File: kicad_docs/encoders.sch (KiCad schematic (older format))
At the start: 40 parts, among them SW1 Rotary_Encoder_Switch, SW2 Rotary_Encoder_Switch, SW3 Rotary_Encoder_Switch, SW4 Rotary_Encoder_Switch

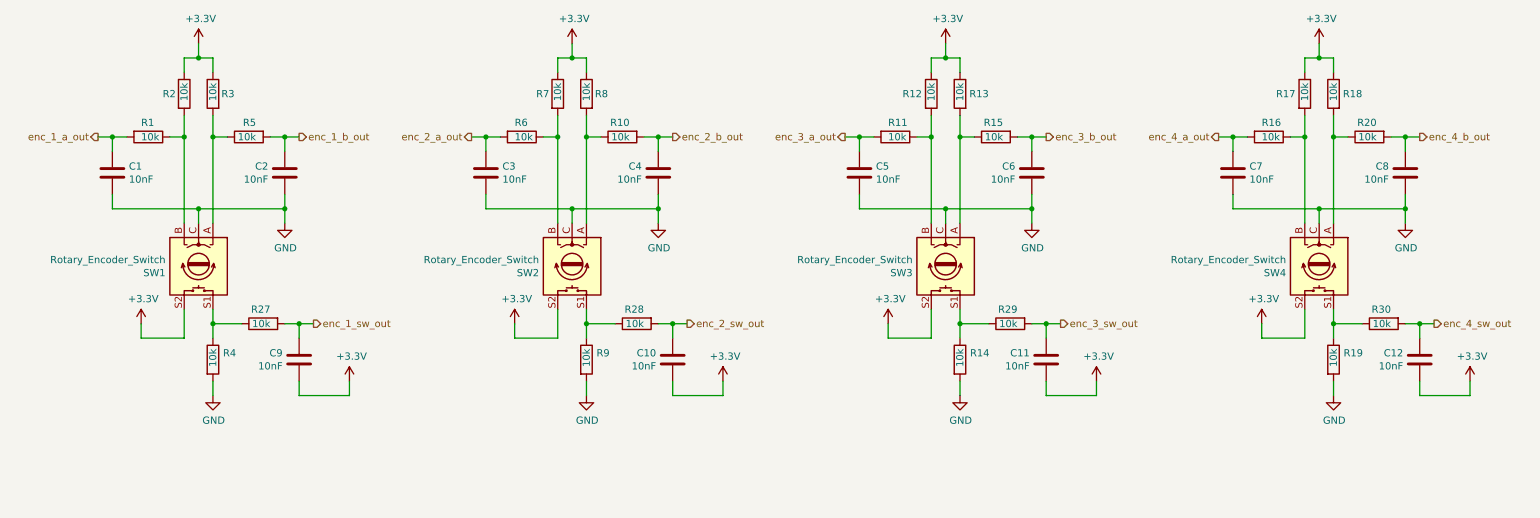
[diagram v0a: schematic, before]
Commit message: change encoder push-button switch passives
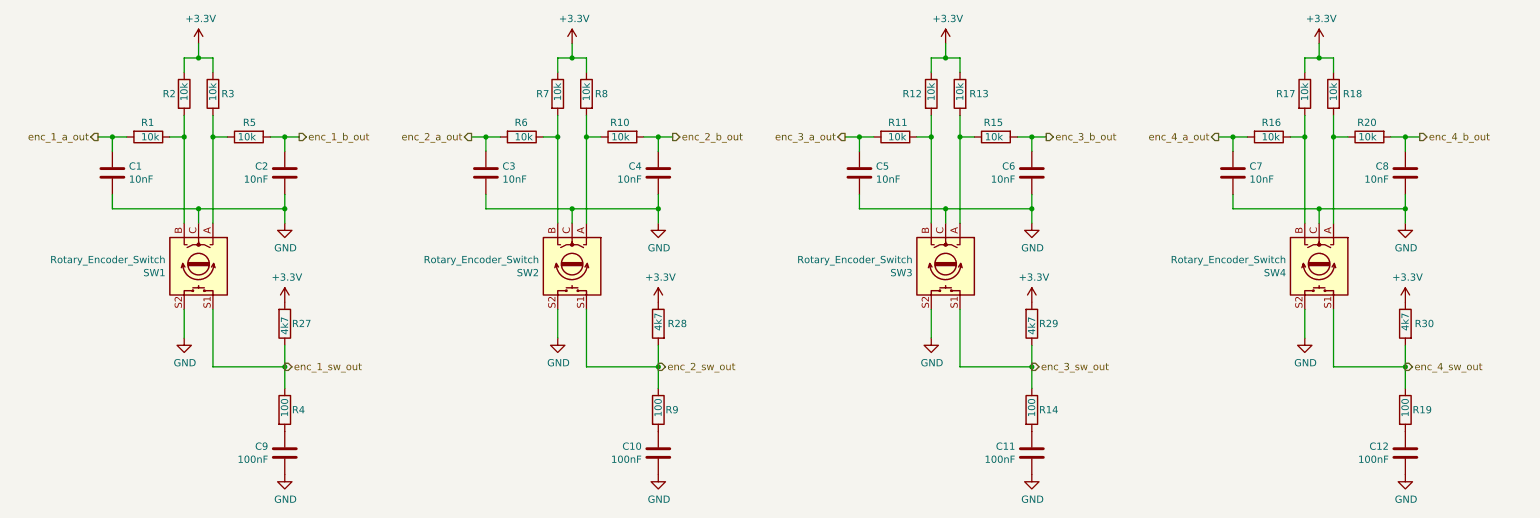
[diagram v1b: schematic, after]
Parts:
- C10, C11, C12, C9: value 10nF -> 100nF
- R14, R19, R4, R9: value 10k -> 100
- R27, R28, R29, R30: value 10k -> 4k7
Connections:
- net +3V3: now also R27.2, R28.1, R29.2, R30.1; no longer C10.2, C11.2, C12.2, C9.2, SW1.S2, SW2.S2, SW3.S2, SW4.S2
- net GND: now also C10.2, C11.2, C12.2, C9.2, SW1.S2, SW2.S2, SW3.S2, SW4.S2; no longer R14.2, R19.2, R4.2, R9.2
- net enc_1_sw_out: now also R27.1, R4.1, SW1.S1; no longer C9.1, R27.2
- net enc_2_sw_out: now also R9.1, SW2.S1; no longer C10.1
- net enc_3_sw_out: now also R14.1, R29.1, SW3.S1; no longer C11.1, R29.2
- net enc_4_sw_out: now also R19.1, SW4.S1; no longer C12.1
- new net: C9.1, R4.2
- new net: C10.1, R9.2
- new net: C11.1, R14.2
- new net: C12.1, R19.2
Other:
- moved on the sheet: C10, C11, C12, C9, R14, R19, R27, R28, R29, R30, R4, R9

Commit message: add EEPROM, big pcb re-design
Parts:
- C1, C12, C2: footprint Capacitor_SMD:C_0805_2012Metric_Pad1.15x1.40mm_HandSolder -> Capacitor_SMD:C_0402_1005Metric
- C10: renamed from C7; footprint Capacitor_SMD:C_0805_2012Metric_Pad1.15x1.40mm_HandSolder -> Capacitor_SMD:C_0402_1005Metric
- C11: renamed from C8; footprint Capacitor_SMD:C_0805_2012Metric_Pad1.15x1.40mm_HandSolder -> Capacitor_SMD:C_0402_1005Metric
- C3: renamed from C9; footprint Capacitor_SMD:C_0805_2012Metric_Pad1.15x1.40mm_HandSolder -> Capacitor_SMD:C_0402_1005Metric
- C4: renamed from C3; footprint Capacitor_SMD:C_0805_2012Metric_Pad1.15x1.40mm_HandSolder -> Capacitor_SMD:C_0402_1005Metric
- C5: renamed from C4; footprint Capacitor_SMD:C_0805_2012Metric_Pad1.15x1.40mm_HandSolder -> Capacitor_SMD:C_0402_1005Metric
- C6: renamed from C10; footprint Capacitor_SMD:C_0805_2012Metric_Pad1.15x1.40mm_HandSolder -> Capacitor_SMD:C_0402_1005Metric
- C7: renamed from C5; footprint Capacitor_SMD:C_0805_2012Metric_Pad1.15x1.40mm_HandSolder -> Capacitor_SMD:C_0402_1005Metric
- C8: renamed from C6; footprint Capacitor_SMD:C_0805_2012Metric_Pad1.15x1.40mm_HandSolder -> Capacitor_SMD:C_0402_1005Metric
- C9: renamed from C11; footprint Capacitor_SMD:C_0805_2012Metric_Pad1.15x1.40mm_HandSolder -> Capacitor_SMD:C_0402_1005Metric
- R1, R10, R2, R3: footprint Resistor_SMD:R_0805_2012Metric_Pad1.15x1.40mm_HandSolder -> Resistor_SMD:R_0402_1005Metric
- R11: renamed from R28; footprint Resistor_SMD:R_0805_2012Metric_Pad1.15x1.40mm_HandSolder -> Resistor_SMD:R_0402_1005Metric
- R12: renamed from R9; footprint Resistor_SMD:R_0805_2012Metric_Pad1.15x1.40mm_HandSolder -> Resistor_SMD:R_0402_1005Metric
- R13: renamed from R11; footprint Resistor_SMD:R_0805_2012Metric_Pad1.15x1.40mm_HandSolder -> Resistor_SMD:R_0402_1005Metric
- R14: renamed from R12; footprint Resistor_SMD:R_0805_2012Metric_Pad1.15x1.40mm_HandSolder -> Resistor_SMD:R_0402_1005Metric
- R15: renamed from R13; footprint Resistor_SMD:R_0805_2012Metric_Pad1.15x1.40mm_HandSolder -> Resistor_SMD:R_0402_1005Metric
- R16: renamed from R15; footprint Resistor_SMD:R_0805_2012Metric_Pad1.15x1.40mm_HandSolder -> Resistor_SMD:R_0402_1005Metric
- R17: renamed from R29; footprint Resistor_SMD:R_0805_2012Metric_Pad1.15x1.40mm_HandSolder -> Resistor_SMD:R_0402_1005Metric
- R18: renamed from R14; footprint Resistor_SMD:R_0805_2012Metric_Pad1.15x1.40mm_HandSolder -> Resistor_SMD:R_0402_1005Metric
- R19: renamed from R16; footprint Resistor_SMD:R_0805_2012Metric_Pad1.15x1.40mm_HandSolder -> Resistor_SMD:R_0402_1005Metric
- R20: renamed from R17; footprint Resistor_SMD:R_0805_2012Metric_Pad1.15x1.40mm_HandSolder -> Resistor_SMD:R_0402_1005Metric
- R21: renamed from R18; footprint Resistor_SMD:R_0805_2012Metric_Pad1.15x1.40mm_HandSolder -> Resistor_SMD:R_0402_1005Metric
- R22: renamed from R20; footprint Resistor_SMD:R_0805_2012Metric_Pad1.15x1.40mm_HandSolder -> Resistor_SMD:R_0402_1005Metric
- R23: renamed from R30; footprint Resistor_SMD:R_0805_2012Metric_Pad1.15x1.40mm_HandSolder -> Resistor_SMD:R_0402_1005Metric
- R24: renamed from R19; footprint Resistor_SMD:R_0805_2012Metric_Pad1.15x1.40mm_HandSolder -> Resistor_SMD:R_0402_1005Metric
- R4: renamed from R5; footprint Resistor_SMD:R_0805_2012Metric_Pad1.15x1.40mm_HandSolder -> Resistor_SMD:R_0402_1005Metric
- R5: renamed from R27; footprint Resistor_SMD:R_0805_2012Metric_Pad1.15x1.40mm_HandSolder -> Resistor_SMD:R_0402_1005Metric
- R6: renamed from R4; footprint Resistor_SMD:R_0805_2012Metric_Pad1.15x1.40mm_HandSolder -> Resistor_SMD:R_0402_1005Metric
- R7: renamed from R6; footprint Resistor_SMD:R_0805_2012Metric_Pad1.15x1.40mm_HandSolder -> Resistor_SMD:R_0402_1005Metric
- R8: renamed from R7; footprint Resistor_SMD:R_0805_2012Metric_Pad1.15x1.40mm_HandSolder -> Resistor_SMD:R_0402_1005Metric
- R9: renamed from R8; footprint Resistor_SMD:R_0805_2012Metric_Pad1.15x1.40mm_HandSolder -> Resistor_SMD:R_0402_1005Metric
- renumbered SW1 to ENC1, SW2 to ENC2, SW3 to ENC3, SW4 to ENC4
